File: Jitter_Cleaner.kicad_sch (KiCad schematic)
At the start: 40 parts, among them J17 MMCX, J20 MMCX, T1 TCM2-43X+, T3 TCM2-43X+, U18 SI5394, U23 74AVC4T245, U26 74LVC8T245, Y1 CX3225SB48000D0FPJC1

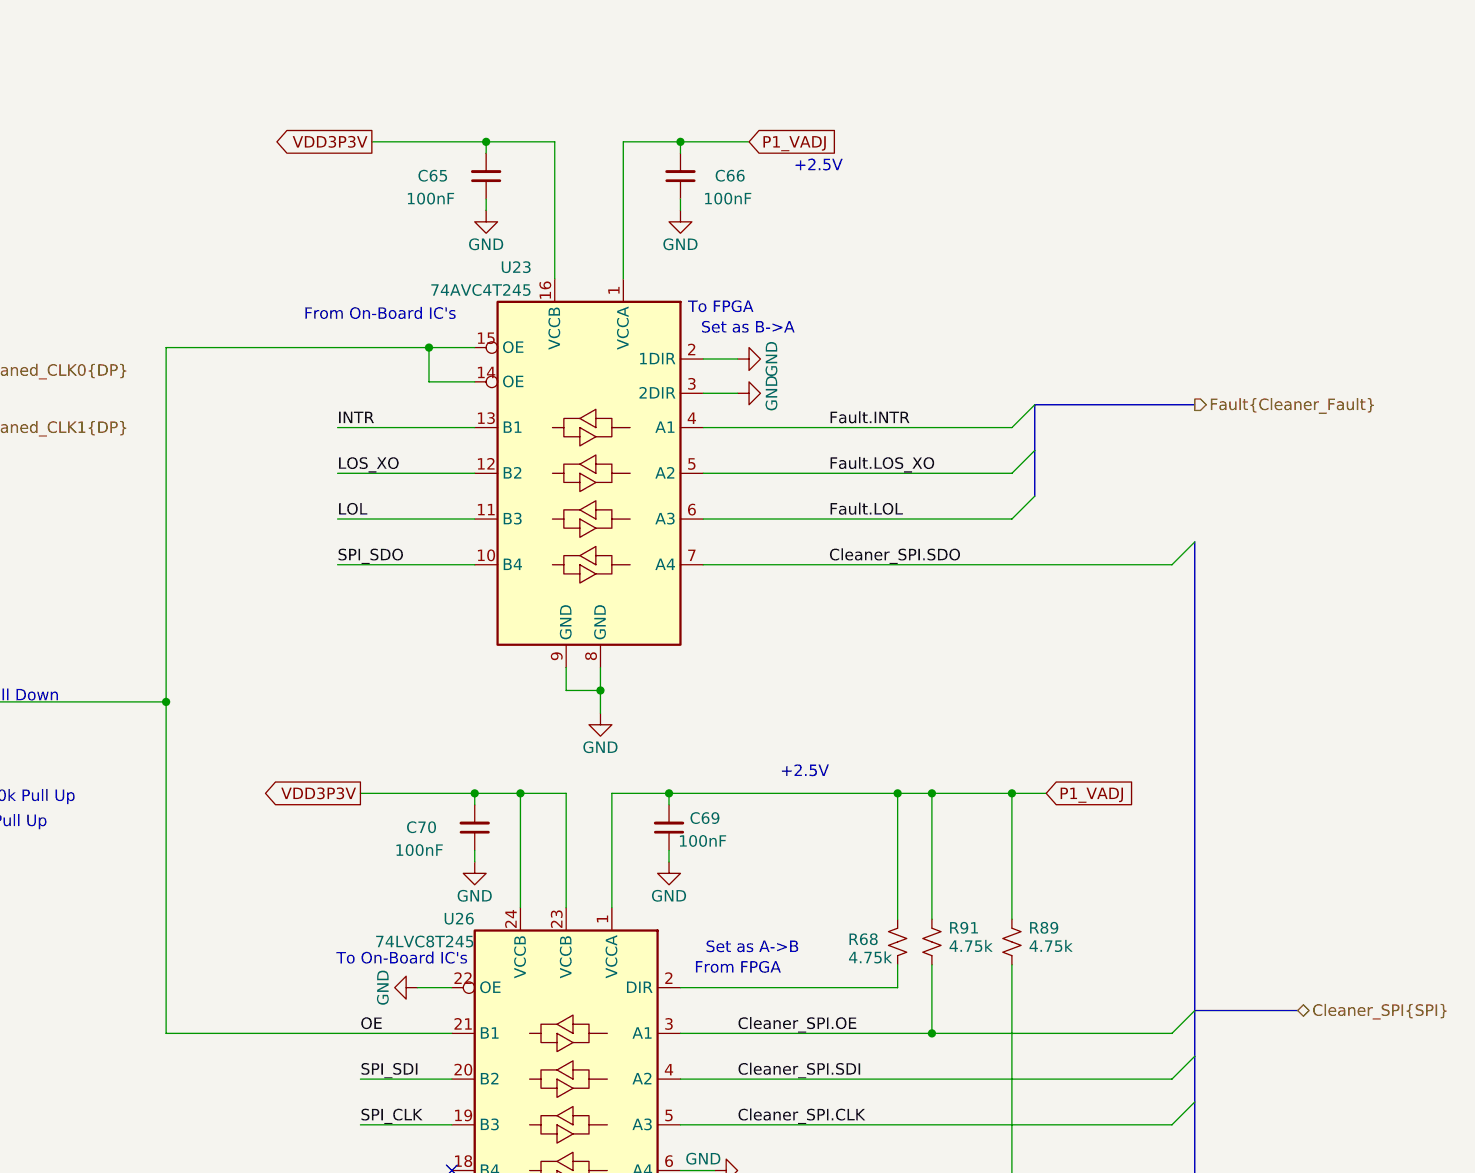
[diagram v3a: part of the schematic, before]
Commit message: Updated Cleaner Control Signaling
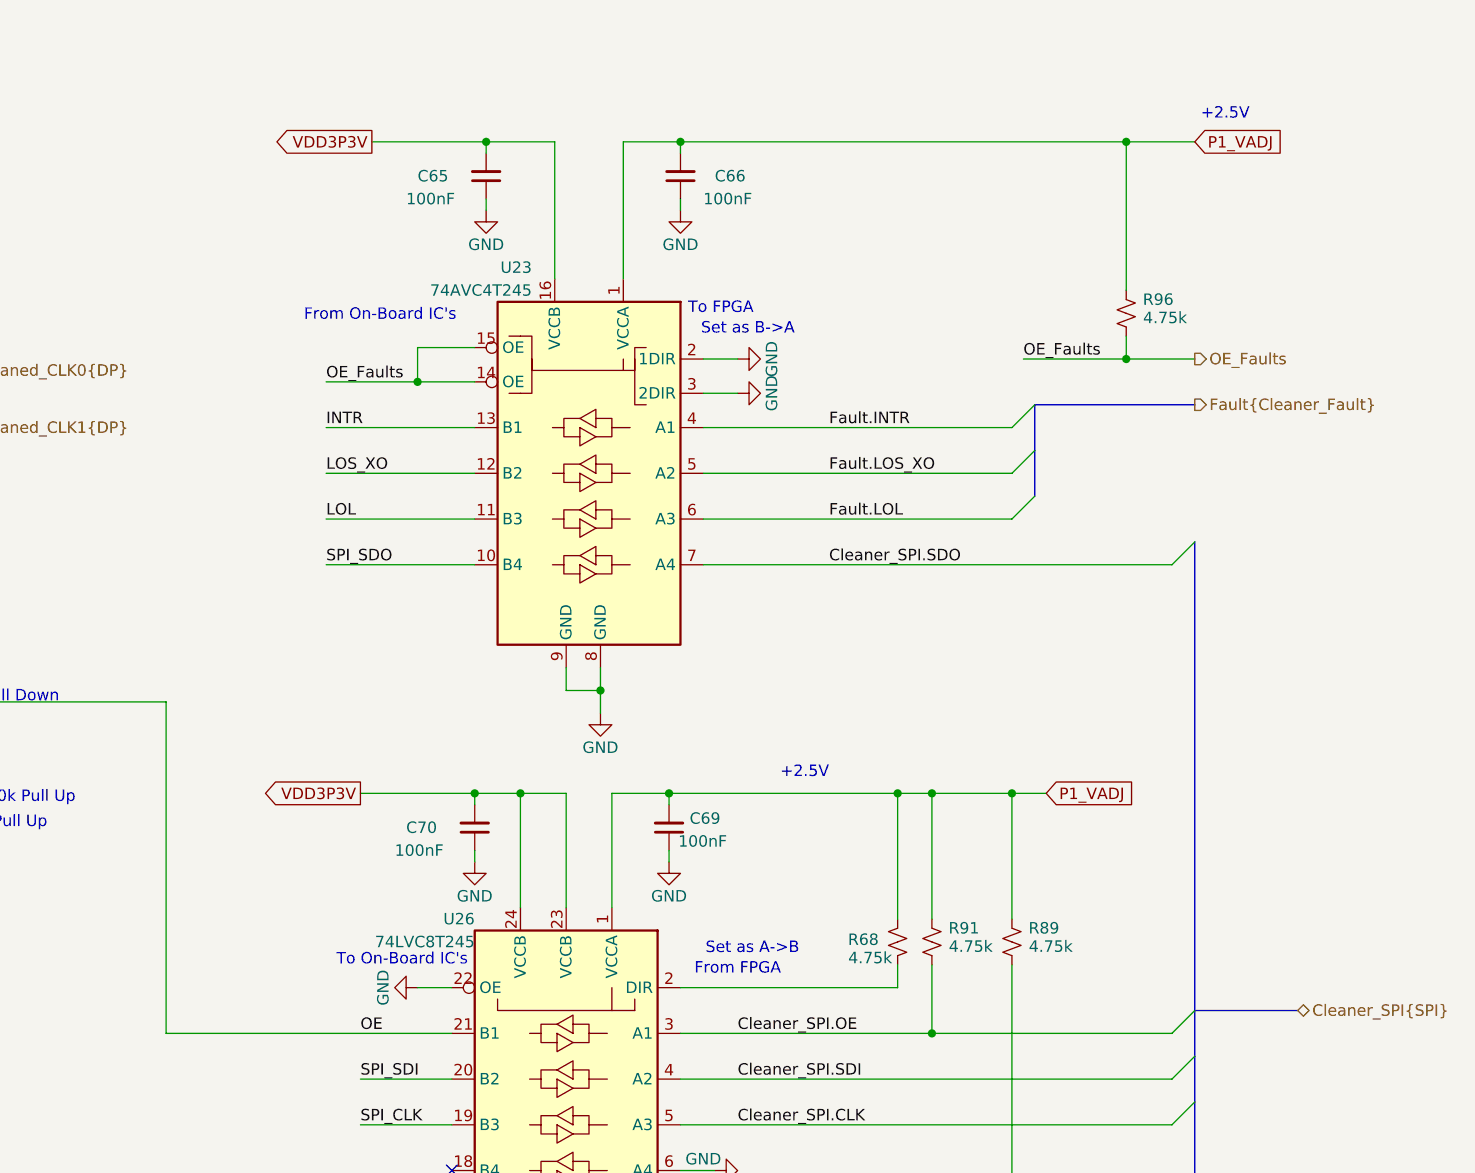
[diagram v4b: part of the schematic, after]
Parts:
- added R96: 4.75k, Resistor_SMD:R_0603_1608Metric, symbol Device:R_Small_US
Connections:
- net OE: no longer U23.14 (OE), U23.15 (OE)
- net P1_VADJ: now also R96.2
- new net OE_Faults: R96.1, U23.14 (OE), U23.15 (OE)
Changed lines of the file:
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@@
 	(text "+2.5V"
 		(exclude_from_sim no)
-		(at 321.564 61.976 0)
+		(at 366.776 56.134 0)
 		(effects
 			(font
@@
 	)
 	(junction
-		(at 246.38 120.65)
+		(at 115.57 48.26)
 		(diameter 0)
 		(color 0 0 0 0)
 	)
 	(junction
-		(at 115.57 48.26)
+		(at 187.96 175.26)
 		(diameter 0)
 		(color 0 0 0 0)
 	)
 	(junction
-		(at 187.96 175.26)
+		(at 158.75 73.66)
 		(diameter 0)
 		(color 0 0 0 0)
 	)
 	(junction
-		(at 158.75 73.66)
+		(at 353.06 82.55)
 		(diameter 0)
 		(color 0 0 0 0)
@@
 	)
 	(junction
-		(at 161.29 73.66)
+		(at 353.06 58.42)
 		(diameter 0)
 		(color 0 0 0 0)
 	)
 	(junction
-		(at 99.06 86.36)
+		(at 161.29 73.66)
 		(diameter 0)
 		(color 0 0 0 0)
 	)
 	(junction
-		(at 138.43 66.04)
+		(at 99.06 86.36)
 		(diameter 0)
 		(color 0 0 0 0)
 	)
 	(junction
-		(at 275.59 81.28)
+		(at 138.43 66.04)
 		(diameter 0)
 		(color 0 0 0 0)
@@
 	)
 	(junction
+		(at 274.32 85.09)
+		(diameter 0)
+		(color 0 0 0 0)
+	)
+	(junction
 		(at 331.47 130.81)
 		(diameter 0)
@@
 	(wire
 		(pts
-			(xy 280.67 85.09) (xy 275.59 85.09)
+			(xy 81.28 119.38) (xy 85.09 119.38)
 		)
 		(stroke
@@
 		)
 	)
-	(wire
+	(bus
 		(pts
-			(xy 81.28 119.38) (xy 85.09 119.38)
+			(xy 215.9 90.17) (xy 215.9 91.44)
 		)
 		(stroke
@@
 		)
 	)
-	(bus
+	(wire
 		(pts
-			(xy 215.9 90.17) (xy 215.9 91.44)
+			(xy 341.63 82.55) (xy 353.06 82.55)
 		)
 		(stroke
@@
 	(wire
 		(pts
+			(xy 280.67 81.28) (xy 274.32 81.28)
+		)
+		(stroke
+			(width 0)
+			(type default)
+		)
+	)
+	(wire
+		(pts
 			(xy 181.61 171.45) (xy 187.96 171.45)
 		)
@@
 	(wire
 		(pts
-			(xy 265.43 100.33) (xy 280.67 100.33)
+			(xy 264.16 100.33) (xy 280.67 100.33)
 		)
 		(stroke
@@
 	(wire
 		(pts
-			(xy 265.43 95.25) (xy 280.67 95.25)
+			(xy 264.16 95.25) (xy 280.67 95.25)
 		)
 		(stroke
@@
 	(wire
 		(pts
-			(xy 265.43 90.17) (xy 280.67 90.17)
+			(xy 264.16 90.17) (xy 280.67 90.17)
 		)
 		(stroke
@@
 	(wire
 		(pts
-			(xy 275.59 85.09) (xy 275.59 81.28)
+			(xy 124.46 55.88) (xy 124.46 57.15)
 		)
 		(stroke
@@
 	(wire
 		(pts
-			(xy 124.46 55.88) (xy 124.46 57.15)
+			(xy 138.43 196.85) (xy 146.05 196.85)
 		)
 		(stroke
@@
 	(wire
 		(pts
-			(xy 138.43 196.85) (xy 146.05 196.85)
+			(xy 142.24 48.26) (xy 153.67 48.26)
 		)
 		(stroke
@@
 	(wire
 		(pts
-			(xy 142.24 48.26) (xy 153.67 48.26)
+			(xy 184.15 109.22) (xy 209.55 109.22)
 		)
 		(stroke
@@
 	(wire
 		(pts
-			(xy 184.15 109.22) (xy 209.55 109.22)
+			(xy 353.06 58.42) (xy 353.06 74.93)
 		)
 		(stroke
@@
 	(wire
 		(pts
-			(xy 303.53 58.42) (xy 311.15 58.42)
+			(xy 274.32 85.09) (xy 280.67 85.09)
+		)
+		(stroke
+			(width 0)
+			(type default)
+		)
+	)
+	(wire
+		(pts
+			(xy 303.53 58.42) (xy 353.06 58.42)
 		)
 		(stroke
@@
 	(wire
 		(pts
+			(xy 274.32 81.28) (xy 274.32 85.09)
+		)
+		(stroke
+			(width 0)
+			(type default)
+		)
+	)
+	(wire
+		(pts
 			(xy 281.94 64.77) (xy 281.94 66.04)
 		)
@@
 	(wire
 		(pts
+			(xy 353.06 82.55) (xy 360.68 82.55)
+		)
+		(stroke
+			(width 0)
+			(type default)
+		)
+	)
+	(wire
+		(pts
 			(xy 290.83 204.47) (xy 290.83 207.01)
 		)
@@
 	(wire
 		(pts
-			(xy 265.43 105.41) (xy 280.67 105.41)
+			(xy 264.16 105.41) (xy 280.67 105.41)
 		)
 		(stroke
@@
 	(wire
 		(pts
+			(xy 264.16 85.09) (xy 274.32 85.09)
+		)
+		(stroke
+			(width 0)
+			(type default)
+		)
+	)
+	(wire
+		(pts
 			(xy 191.77 48.26) (xy 182.88 48.26)
 		)
@@
 	(wire
 		(pts
-			(xy 194.31 167.64) (xy 194.31 180.34)
+			(xy 353.06 58.42) (xy 360.68 58.42)
 		)
 		(stroke
@@
 	(wire
 		(pts
-			(xy 294.64 207.01) (xy 290.83 207.01)
+			(xy 194.31 167.64) (xy 194.31 180.34)
 		)
 		(stroke
@@
 	(wire
 		(pts
-			(xy 95.25 127) (xy 95.25 121.92)
+			(xy 294.64 207.01) (xy 290.83 207.01)
 		)
 		(stroke
@@
 	(wire
 		(pts
-			(xy 124.46 66.04) (xy 124.46 68.58)
+			(xy 95.25 127) (xy 95.25 121.92)
 		)
 		(stroke
@@
 	(wire
 		(pts
-			(xy 246.38 81.28) (xy 275.59 81.28)
+			(xy 124.46 66.04) (xy 124.46 68.58)
 		)
 		(stroke
@@
 	(wire
 		(pts
+			(xy 353.06 80.01) (xy 353.06 82.55)
+		)
+		(stroke
+			(width 0)
+			(type default)
+		)
+	)
+	(wire
+		(pts
 			(xy 163.83 73.66) (xy 163.83 78.74)
 		)
@@
 	(wire
 		(pts
-			(xy 280.67 81.28) (xy 275.59 81.28)
-		)
-		(stroke
-			(width 0)
-			(type default)
-		)
-	)
-	(wire
-		(pts
 			(xy 181.61 64.77) (xy 181.61 67.31)
 		)
@@
 	(wire
 		(pts
-			(xy 246.38 81.28) (xy 246.38 120.65)
-		)
-		(stroke
-			(width 0)
-			(type default)
-		)
-	)
-	(wire
-		(pts
 			(xy 278.13 152.4) (xy 274.32 152.4)
 		)
@@
 	)
 	(label "LOS_XO"
-		(at 265.43 95.25 0)
+		(at 264.16 95.25 0)
 		(effects
 			(font
@@
 	)
 	(label "INTR"
-		(at 265.43 90.17 0)
+		(at 264.16 90.17 0)
 		(effects
 			(font
@@
 	)
 	(label "SPI_SDO"
-		(at 265.43 105.41 0)
+		(at 264.16 105.41 0)
 		(effects
 			(font
@@
 		)
 	)
+	(label "OE_Faults"
+		(at 341.63 82.55 0)
+		(effects
+			(font
+				(size 1.27 1.27)
+			)
+			(justify left bottom)
+		)
+	)
 	(label "SPI_SDO"
 		(at 213.36 129.54 180)
@@
 	)
 	(label "LOL"
-		(at 265.43 100.33 0)
+		(at 264.16 100.33 0)
 		(effects
 			(font
@@
 		)
 	)
+	(label "OE_Faults"
+		(at 264.16 85.09 0)
+		(effects
+			(font
+				(size 1.27 1.27)
+			)
+			(justify left bottom)
+		)
+	)
 	(label "Fault.LOS_XO"
 		(at 320.04 95.25 0)
@@
 	(global_label "P1_VADJ"
 		(shape input)
-		(at 311.15 58.42 0)
+		(at 360.68 58.42 0)
 		(fields_autoplaced yes)
 		(effects
@@
 		)
 		(property "Intersheetrefs" "${INTERSHEET_REFS}"
-			(at 321.9971 58.42 0)
+			(at 371.5271 58.42 0)
 			(effects
 				(font
@@
 		)
 	)
+	(hierarchical_label "OE_Faults"
+		(shape output)
+		(at 360.68 82.55 0)
+		(effects
+			(font
+				(size 1.27 1.27)
+			)
+			(justify left)
+		)
+	)
 	(hierarchical_label "Cleaned_CLK1{DP}"
 		(shape output)
@@
 					(unit 1)
 				)
+			)
+		)
+	)
+	(symbol
+		(lib_id "Device:R_Small_US")
+		(at 353.06 77.47 180)
+		(unit 1)
+		(exclude_from_sim no)
+		(in_bom yes)
+		(on_board yes)
+		(dnp no)
+		(property "Reference" "R96"
+			(at 356.616 75.946 0)
+			(effects
+				(font
+					(size 1.27 1.27)
+				)
+			)
+		)
+		(property "Value" "4.75k"
+			(at 357.378 77.978 0)
+			(effects
+				(font
+					(size 1.27 1.27)
+				)
+			)
+		)
+		(property "Footprint" "Resistor_SMD:R_0603_1608Metric"
+			(at 353.06 77.47 0)
+			(effects
+				(font
+					(size 1.27 1.27)
+				)
+				(hide yes)
+			)
+		)
+		(property "Datasheet" "~"
+			(at 353.06 77.47 0)
+			(effects
+				(font
+					(size 1.27 1.27)
+				)
+				(hide yes)
+			)
+		)
+		(property "Description" "RES 4.75K OHM 1% 1/10W 0603"
+			(at 353.06 77.47 0)
+			(effects
+				(font
+					(size 1.27 1.27)
+				)
+				(hide yes)
+			)
+		)
+		(property "MPN" "RC0603FR-134K75L"
+			(at 353.06 77.47 90)
+			(effects
+				(font
+					(size 1.27 1.27)
+				)
+				(hide yes)
+			)
+		)
+		(property "Manufacturer" "Yageo"
+			(at 353.06 77.47 0)
+			(effects
+				(font
+					(size 1.27 1.27)
+				)
+				(hide yes)
+			)
+		)
+		(pin "1"
+		)
+		(pin "2"
+		)
+		(instances
+			(project "evr-fmc"
+				(path "/1719e569-47c8-4fa0-8523-9c9686ef0dba/51b6ba02-2a45-47f9-920d-b1129f765b02"
+					(reference "R96")
+					(unit 1)
+				)
+				(path "/1719e569-47c8-4fa0-8523-9c9686ef0dba/72a6e05f-9d23-47d7-93ac-d48e996d2022"
+					(reference "R96")
+					(unit 1)
+				)

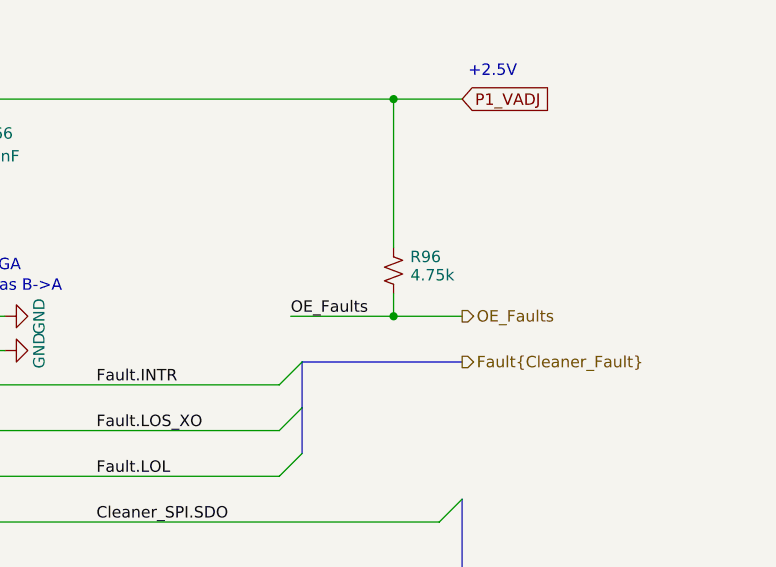
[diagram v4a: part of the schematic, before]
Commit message: Schematic Updates
-Added Heartbeat LED
-Assigned Jitter cleaner OE to FPGA pins
-Changed LDO parts
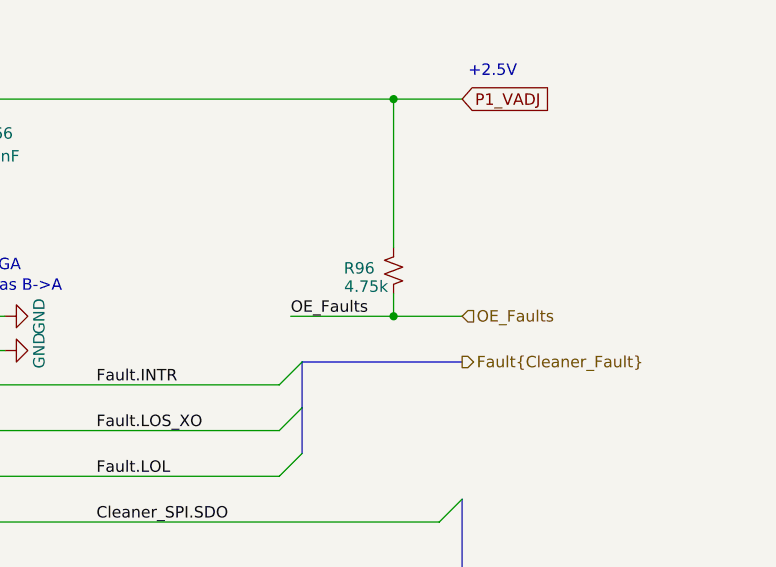
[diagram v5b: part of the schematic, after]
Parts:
- R96: footprint Resistor_SMD:R_0603_1608Metric -> Resistor_SMD:R_0402_1005Metric; MPN RC0603FR-134K75L -> RC0402FR-074K75L; Manufacturer Yageo -> (none)
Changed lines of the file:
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@@
 	)
 	(hierarchical_label "OE_Faults"
-		(shape output)
+		(shape input)
 		(at 360.68 82.55 0)
 		(effects
@@
 	)
 	(symbol
+		(lib_id "Device:R_Small_US")
+		(at 353.06 77.47 0)
+		(mirror x)
+		(unit 1)
+		(exclude_from_sim no)
+		(in_bom yes)
+		(on_board yes)
+		(dnp no)
+		(property "Reference" "R96"
+			(at 349.25 77.216 0)
+			(effects
+				(font
+					(size 1.27 1.27)
+				)
+			)
+		)
+		(property "Value" "4.75k"
+			(at 350.012 79.248 0)
+			(effects
+				(font
+					(size 1.27 1.27)
+				)
+			)
+		)
+		(property "Footprint" "Resistor_SMD:R_0402_1005Metric"
+			(at 353.06 77.47 0)
+			(effects
+				(font
+					(size 1.27 1.27)
+				)
+				(hide yes)
+			)
+		)
+		(property "Datasheet" "~"
+			(at 353.06 77.47 0)
+			(effects
+				(font
+					(size 1.27 1.27)
+				)
+				(hide yes)
+			)
+		)
+		(property "Description" ""
+			(at 353.06 77.47 0)
+			(effects
+				(font
+					(size 1.27 1.27)
+				)
+				(hide yes)
+			)
+		)
+		(property "MPN" "RC0402FR-074K75L"
+			(at 353.06 77.47 90)
+			(effects
+				(font
+					(size 1.27 1.27)
+				)
+				(hide yes)
+			)
+		)
+		(pin "1"
+		)
+		(pin "2"
+		)
+		(instances
+			(project "evr-fmc"
+				(path "/1719e569-47c8-4fa0-8523-9c9686ef0dba/51b6ba02-2a45-47f9-920d-b1129f765b02"
+					(reference "R97")
+					(unit 1)
+				)
+				(path "/1719e569-47c8-4fa0-8523-9c9686ef0dba/72a6e05f-9d23-47d7-93ac-d48e996d2022"
+					(reference "R96")
+					(unit 1)
+				)
+			)
+		)
+	)
+	(symbol
 		(lib_id "power:GND")
 		(at 133.35 74.93 0)
@@
 					(unit 1)
 				)
-			)
-		)
-	)
-	(symbol
-		(lib_id "Device:R_Small_US")
-		(at 353.06 77.47 180)
-		(unit 1)
-		(exclude_from_sim no)
-		(in_bom yes)
-		(on_board yes)
-		(dnp no)
-		(property "Reference" "R96"
-			(at 356.616 75.946 0)
-			(effects
-				(font
-					(size 1.27 1.27)
-				)
-			)
-		)
-		(property "Value" "4.75k"
-			(at 357.378 77.978 0)
-			(effects
-				(font
-					(size 1.27 1.27)
-				)
-			)
-		)
-		(property "Footprint" "Resistor_SMD:R_0603_1608Metric"
-			(at 353.06 77.47 0)
-			(effects
-				(font
-					(size 1.27 1.27)
-				)
-				(hide yes)
-			)
-		)
-		(property "Datasheet" "~"
-			(at 353.06 77.47 0)
-			(effects
-				(font
-					(size 1.27 1.27)
-				)
-				(hide yes)
-			)
-		)
-		(property "Description" "RES 4.75K OHM 1% 1/10W 0603"
-			(at 353.06 77.47 0)
-			(effects
-				(font
-					(size 1.27 1.27)
-				)
-				(hide yes)
-			)
-		)
-		(property "MPN" "RC0603FR-134K75L"
-			(at 353.06 77.47 90)
-			(effects
-				(font
-					(size 1.27 1.27)
-				)
-				(hide yes)
-			)
-		)
-		(property "Manufacturer" "Yageo"
-			(at 353.06 77.47 0)
-			(effects
-				(font
-					(size 1.27 1.27)
-				)
-				(hide yes)
-			)
-		)
-		(pin "1"
-		)
-		(pin "2"
-		)
-		(instances
-			(project "evr-fmc"
-				(path "/1719e569-47c8-4fa0-8523-9c9686ef0dba/51b6ba02-2a45-47f9-920d-b1129f765b02"
-					(reference "R96")
-					(unit 1)
-				)
-				(path "/1719e569-47c8-4fa0-8523-9c9686ef0dba/72a6e05f-9d23-47d7-93ac-d48e996d2022"
-					(reference "R96")
-					(unit 1)
-				)
